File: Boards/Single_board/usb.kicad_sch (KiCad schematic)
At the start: 2 parts, among them J3 USB_C_Receptacle_USB2.0_16P, U3 CH340G

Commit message: Single board nearly ready to order
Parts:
- removed U3: CH340G, Package_SO:SOIC-16_3.9x9.9mm_P1.27mm, symbol Interface_USB:CH340G
- added C6: 4.7uF, Capacitor_SMD:C_0805_2012Metric, symbol Device:C_Small
- added C7, C8, C9: 100nF, Capacitor_SMD:C_0805_2012Metric, symbol Device:C_Small
- added D34: SD101AWS, Diode_SMD:D_SOD-323, symbol Device:D_Small
- added R44, R45: 5.1k, Resistor_SMD:R_0603_1608Metric, symbol Device:R_Small
- added R46, R47: 1k, Resistor_SMD:R_0603_1608Metric, symbol Device:R_Small
- added U3: CH340C, Package_SO:SOIC-16_3.9x9.9mm_P1.27mm, symbol Interface_USB:CH340C
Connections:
- net GND: now reaches J3.A1 (GND), J3.A12 (GND), J3.B1 (GND), J3.B12 (GND)
- net GND: now also J3.S1 (SHIELD), C6.2, C7.2, C9.2, R44.1, R45.1, U3.1 (GND)
- net at J3.A4 (VBUS), J3.A9 (VBUS), J3.B4 (VBUS)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: now also D34.2 (A)
- net at J3.A5 (CC1): now also R44.2
- net at J3.A6 (D+): now also J3.B6 (D+), U3.5 (UD+)
- net at J3.A7 (D-): now also J3.B7 (D-), U3.6 (UD-)
- net at J3.B5 (CC2): now also R45.2
- new net: C9.1, U3.4 (V3)
- new net: R46.2, U3.2 (TXD)
- new net: C8.1, U3.13 (~{DTR})
- new net: R47.2, U3.3 (RXD)
- new net +5V: C6.1, C7.1, D34.1 (K), U3.16 (VCC)
- new net RESET: C8.2
- new net USB_RX: R47.1
- new net USB_TX: R46.1
- no-connect marks 0 -> 9

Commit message: Fixes on single board
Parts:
- D34: value SD101AWS -> MBR0520LT1G; footprint Diode_SMD:D_SOD-323 -> Diode_SMD:D_SOD-123
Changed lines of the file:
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@@
 			)
 		)
-		(property "Value" "SD101AWS"
+		(property "Value" "MBR0520LT1G"
 			(at 124.46 44.45 0)
 			(effects
@@
 			)
 		)
-		(property "Footprint" "Diode_SMD:D_SOD-323"
+		(property "Footprint" "Diode_SMD:D_SOD-123"
 			(at 124.46 48.26 90)
 			(effects

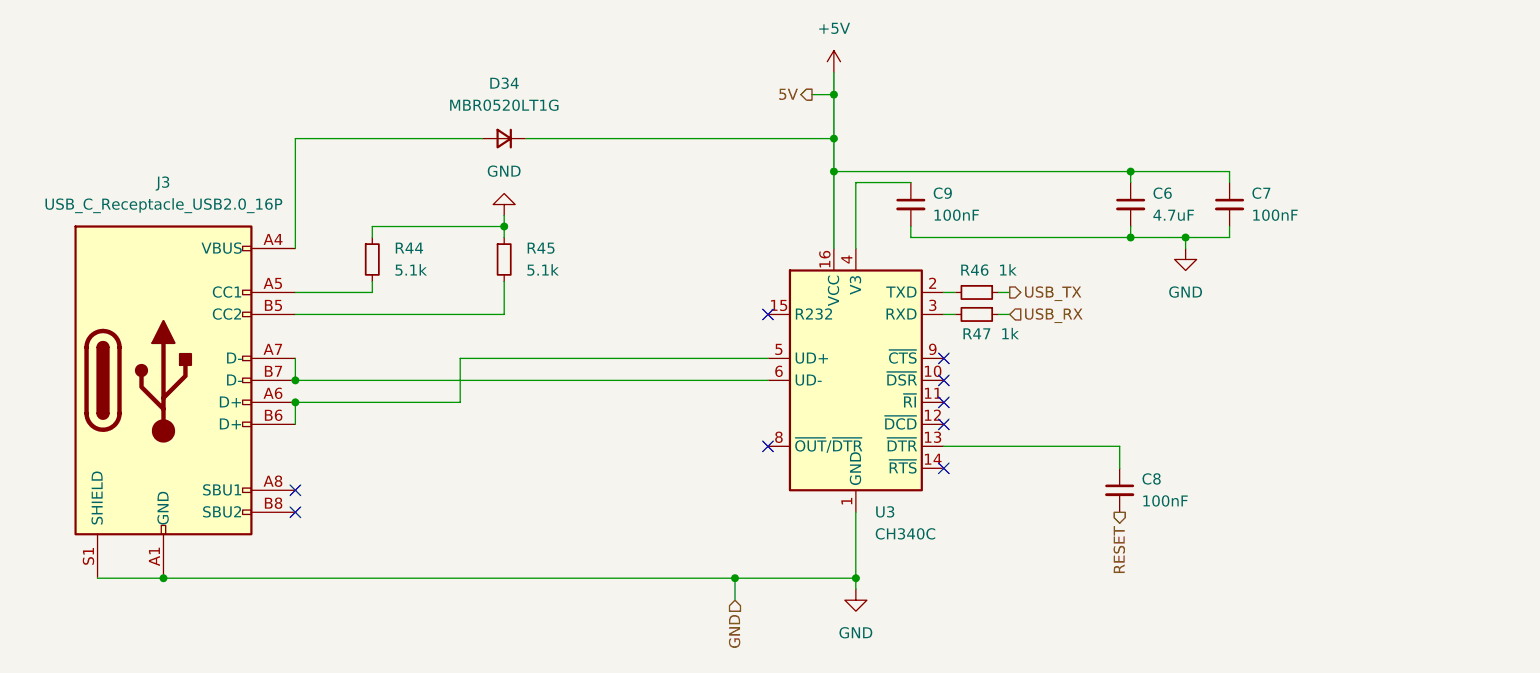
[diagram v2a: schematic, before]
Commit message: Re-stitch and clean up redundant tracks.  Correct some port directions.
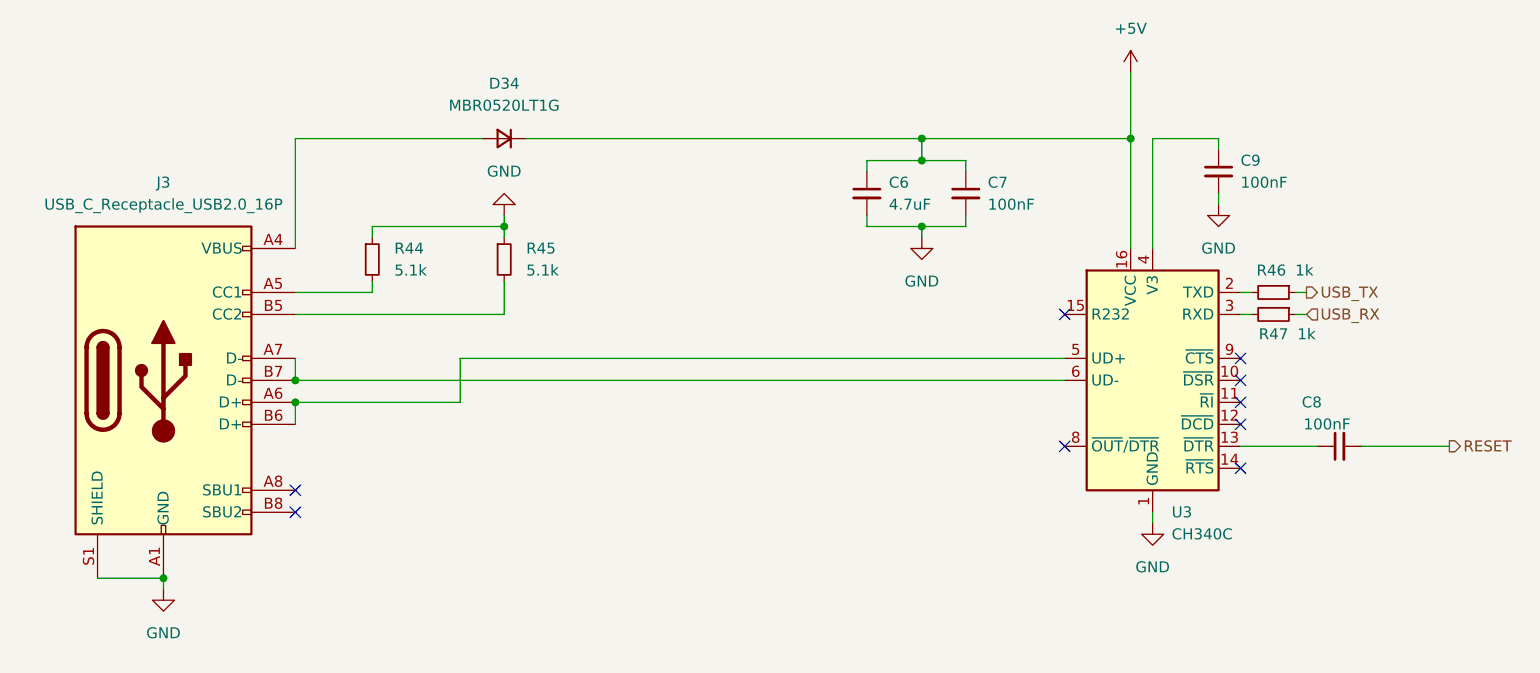
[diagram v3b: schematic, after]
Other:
- moved on the sheet: C6, C7, C8, C9, R46, R47, U3

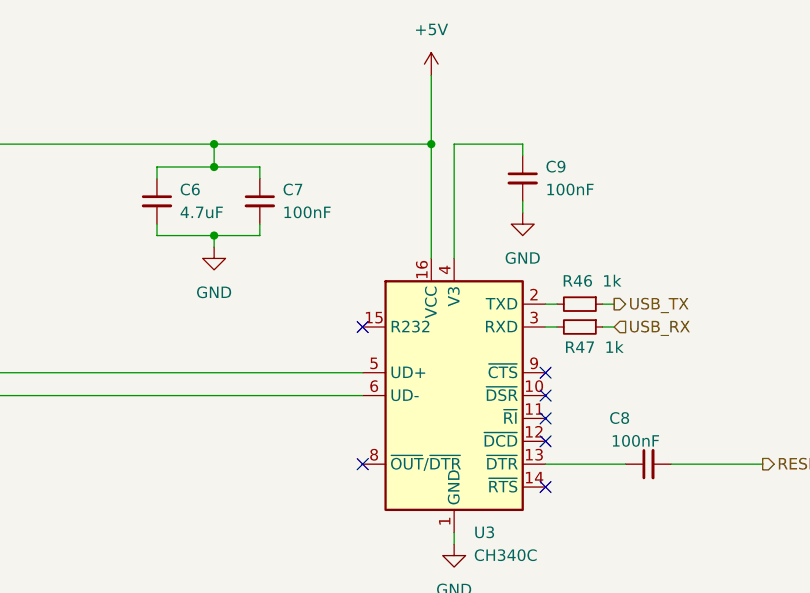
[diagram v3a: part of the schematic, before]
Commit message: Arrange and place components
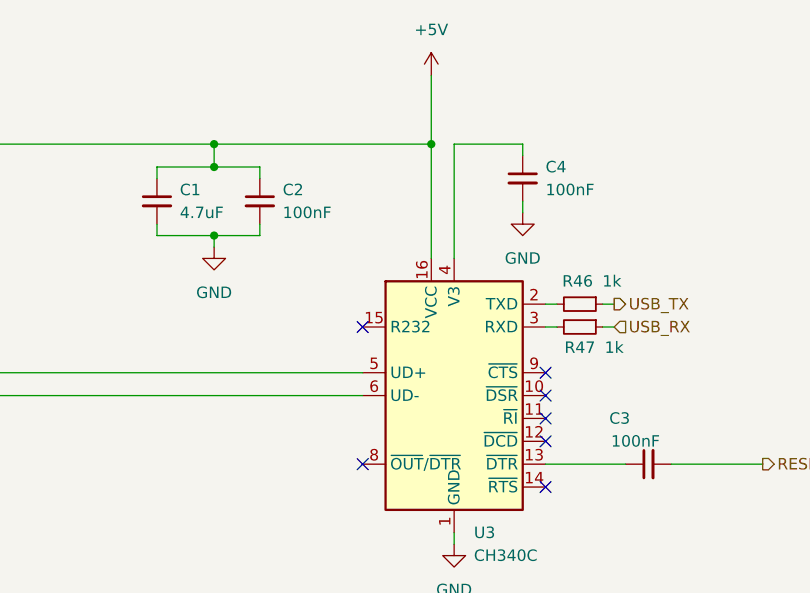
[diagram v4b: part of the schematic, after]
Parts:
- renumbered C6 to C1, C7 to C2, C8 to C3, C9 to C4
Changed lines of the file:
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@@
 		(dnp no)
 		(fields_autoplaced yes)
-		(property "Reference" "C6"
+		(property "Reference" "C1"
 			(at 168.91 53.3462 0)
 			(effects
@@
 			(project "Single_board"
 				(path "/f30854c1-5bc2-470d-aabe-1768a5b01b46/2c846281-f7ac-4d2e-99f9-816b435af6ae"
-					(reference "C6")
+					(reference "C1")
 					(unit 1)
 				)
@@
 		(dnp no)
 		(fields_autoplaced yes)
-		(property "Reference" "C9"
+		(property "Reference" "C4"
 			(at 209.55 50.8062 0)
 			(effects
@@
 			(project "Single_board"
 				(path "/f30854c1-5bc2-470d-aabe-1768a5b01b46/2c846281-f7ac-4d2e-99f9-816b435af6ae"
-					(reference "C9")
+					(reference "C4")
 					(unit 1)
 				)
@@
 		(on_board yes)
 		(dnp no)
-		(property "Reference" "C7"
+		(property "Reference" "C2"
 			(at 180.34 53.3462 0)
 			(effects
@@
 			(project "Single_board"
 				(path "/f30854c1-5bc2-470d-aabe-1768a5b01b46/2c846281-f7ac-4d2e-99f9-816b435af6ae"
-					(reference "C7")
+					(reference "C2")
 					(unit 1)
 				)
@@
 		(on_board yes)
 		(dnp no)
-		(property "Reference" "C8"
+		(property "Reference" "C3"
 			(at 218.948 78.74 90)
 			(effects
@@
 			(project "Single_board"
 				(path "/f30854c1-5bc2-470d-aabe-1768a5b01b46/2c846281-f7ac-4d2e-99f9-816b435af6ae"
-					(reference "C8")
-					(unit 1)
-				)
+					(reference "C3")
+					(unit 1)
+				)
